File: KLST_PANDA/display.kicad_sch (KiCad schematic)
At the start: 10 parts, among them IC1 CAT4139TD-GT3, J6 FPC-40

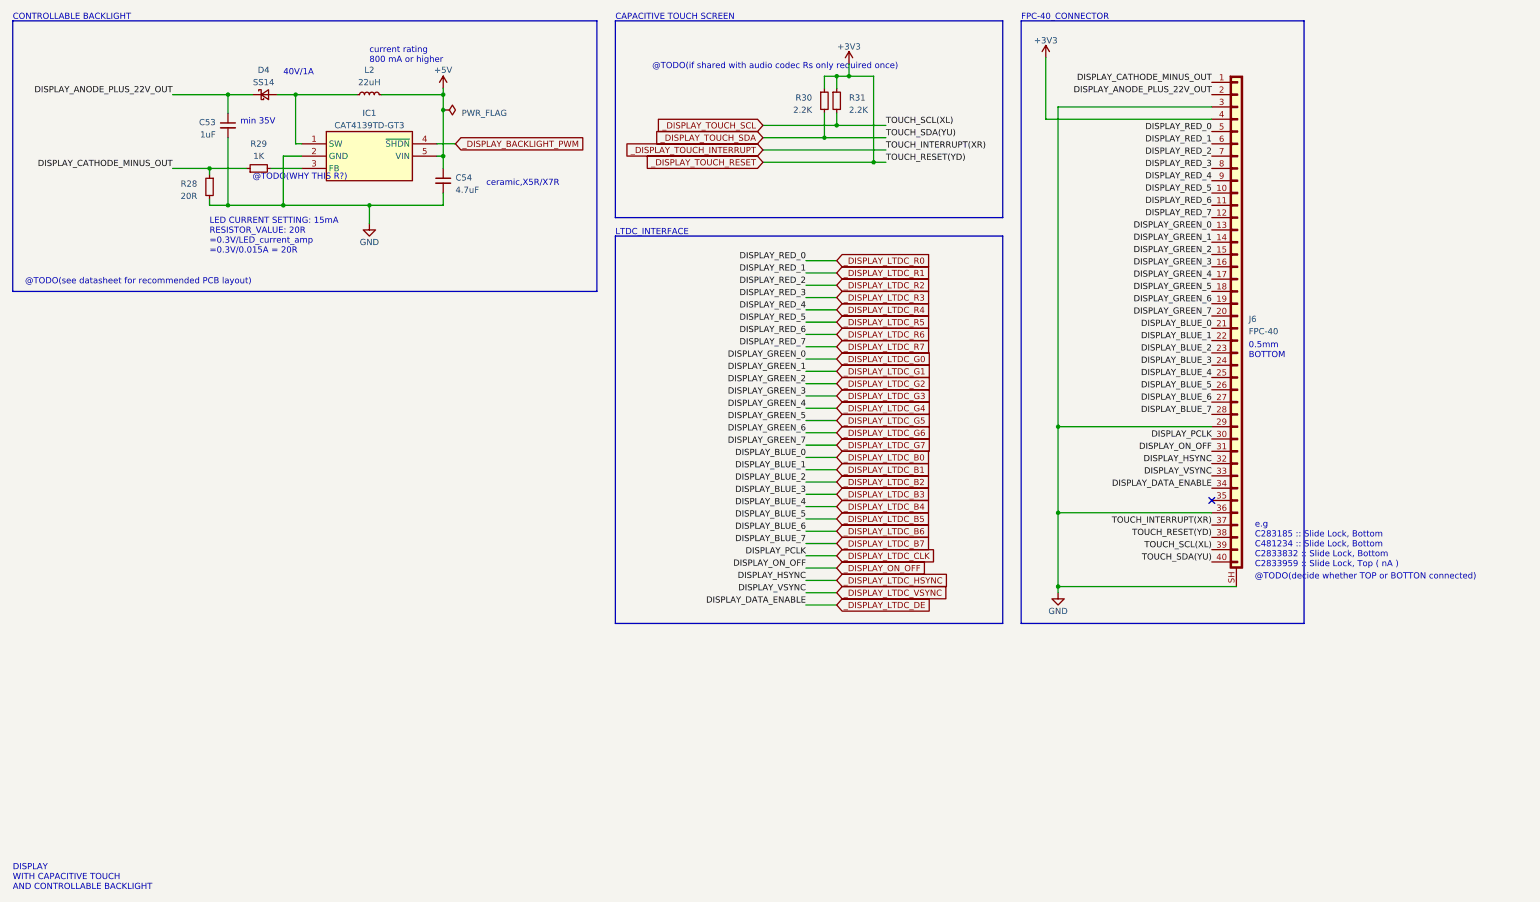
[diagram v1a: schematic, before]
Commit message: removed DRC warnings and error, added power page
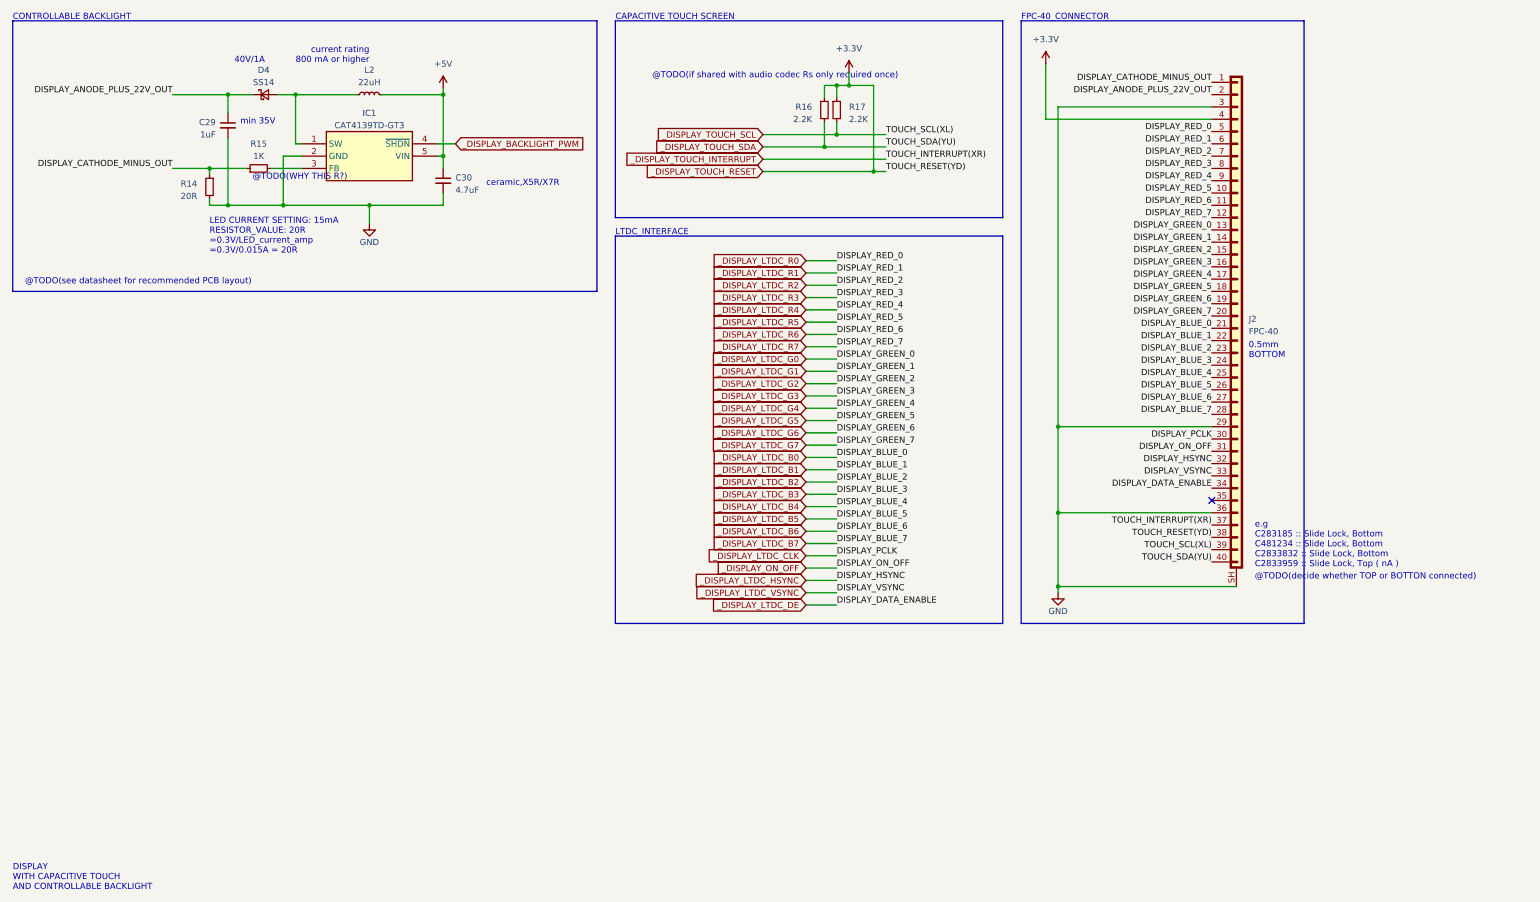
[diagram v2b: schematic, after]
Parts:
- renumbered C53 to C29, C54 to C30, J6 to J2, R28 to R14, R29 to R15, R30 to R16, R31 to R17
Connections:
- net +3V3 renamed +3.3V
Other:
- moved on the sheet: R16, R17

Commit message: changed I2C label, display can now be switched on and off
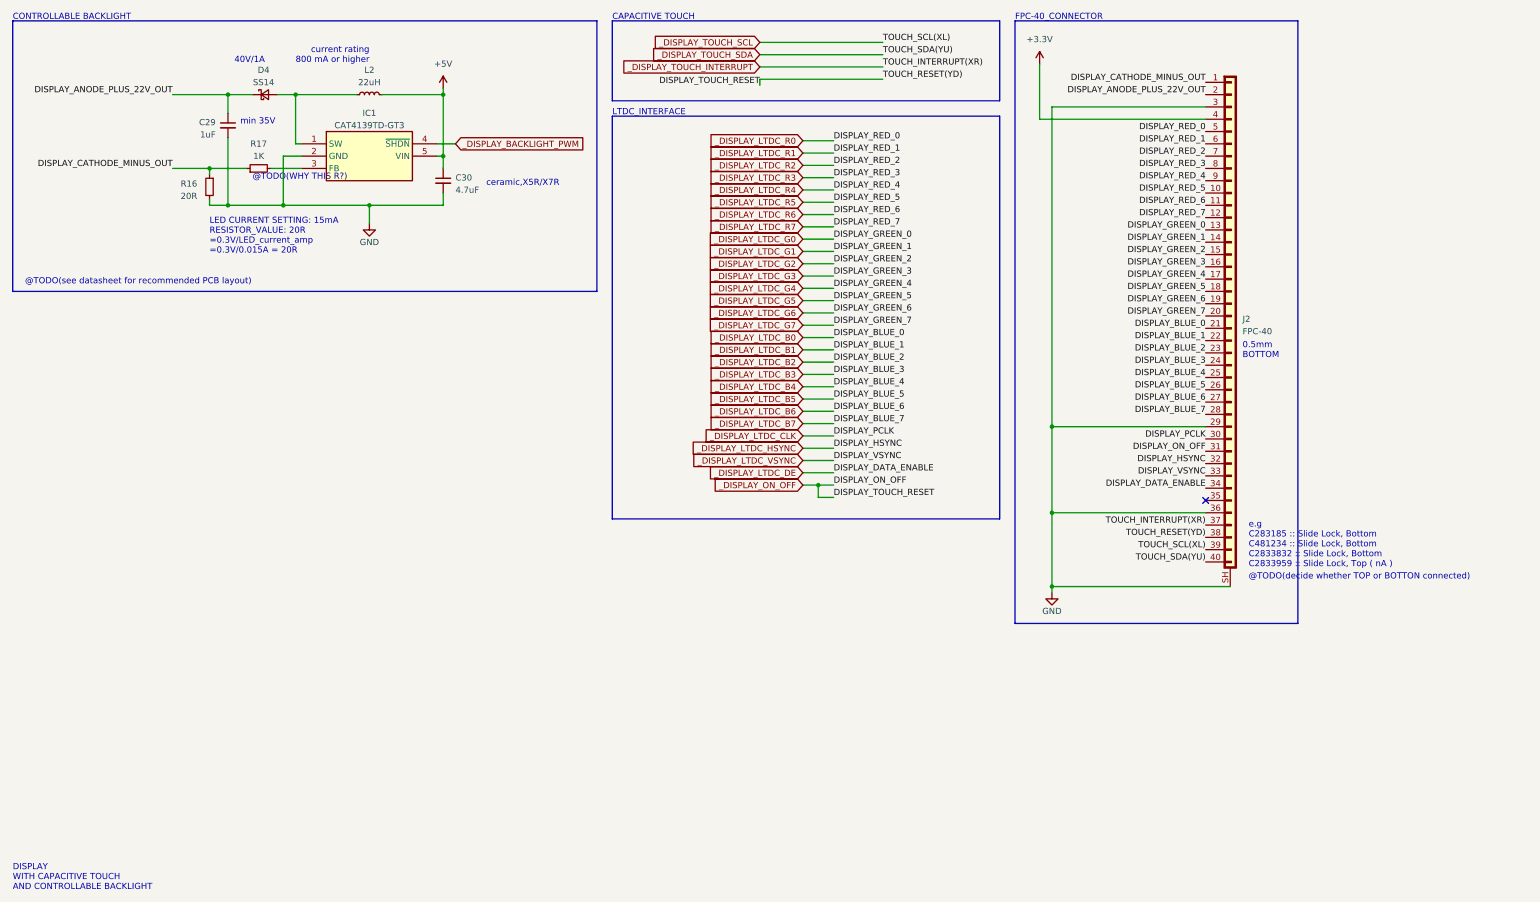
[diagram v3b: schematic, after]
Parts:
- removed R16, R17: 2.2K, symbol Device:R_Small
- renumbered R14 to R16, R15 to R17
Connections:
- net +3.3V: no longer J2.38 (Pin_38)
- net _DISPLAY_ON_OFF: now also J2.38 (Pin_38)
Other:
- note added: "CAPACITIVE TOUCH"
- note removed: "@TODO(if shared with audio codec Rs only required once)"
- note removed: "CAPACITIVE TOUCH SCREEN"
- moved on the sheet: J2

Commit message: cleaned up
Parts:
- renumbered R16 to R18, R17 to R19
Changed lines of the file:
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@@
   (symbol (lib_id "power:+5V") (at 104.14 29.21 0) (unit 1)
     (in_bom yes) (on_board yes) (dnp no) (fields_autoplaced)
-    (property "Reference" "#PWR043" (at 104.14 33.02 0)
+    (property "Reference" "#PWR044" (at 104.14 33.02 0)
       (effects (font (size 1.27 1.27)) hide)
     )
@@
       (project "KLST_PANDA"
         (path "/b4513875-4c57-4720-bcc5-43ead67fe18f/e5470bb0-cacd-4f1d-9ba6-63c7432dbe78"
-          (reference "#PWR043") (unit 1)
+          (reference "#PWR044") (unit 1)
         )
       )
@@
         )
         (path "/b4513875-4c57-4720-bcc5-43ead67fe18f/e5470bb0-cacd-4f1d-9ba6-63c7432dbe78"
-          (reference "#PWR045") (unit 1)
+          (reference "#PWR046") (unit 1)
         )
       )
@@
   (symbol (lib_id "Device:R_Small") (at 66.04 45.72 90) (unit 1)
     (in_bom yes) (on_board yes) (dnp no) (fields_autoplaced)
-    (property "Reference" "R17" (at 66.04 40.64 90)
+    (property "Reference" "R19" (at 66.04 40.64 90)
       (effects (font (size 1.27 1.27)))
     )
@@
       (project "KLST_PANDA"
         (path "/b4513875-4c57-4720-bcc5-43ead67fe18f/e5470bb0-cacd-4f1d-9ba6-63c7432dbe78"
-          (reference "R17") (unit 1)
+          (reference "R19") (unit 1)
         )
       )
@@
         )
         (path "/b4513875-4c57-4720-bcc5-43ead67fe18f/e5470bb0-cacd-4f1d-9ba6-63c7432dbe78"
-          (reference "#PWR044") (unit 1)
+          (reference "#PWR045") (unit 1)
         )
       )
@@
   (symbol (lib_id "Device:R_Small") (at 55.88 49.53 0) (mirror y) (unit 1)
     (in_bom yes) (on_board yes) (dnp no)
-    (property "Reference" "R16" (at 53.34 48.895 0)
+    (property "Reference" "R18" (at 53.34 48.895 0)
       (effects (font (size 1.27 1.27)) (justify left))
     )
@@
       (project "KLST_PANDA"
         (path "/b4513875-4c57-4720-bcc5-43ead67fe18f/e5470bb0-cacd-4f1d-9ba6-63c7432dbe78"
-          (reference "R16") (unit 1)
+          (reference "R18") (unit 1)
         )
       )
@@
         )
         (path "/b4513875-4c57-4720-bcc5-43ead67fe18f/e5470bb0-cacd-4f1d-9ba6-63c7432dbe78"
-          (reference "#PWR042") (unit 1)
-        )
-      )
+          (reference "#PWR043") (unit 1)
+        )
+      )

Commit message: unified internal I2C bus, cleaned up, added ESD protection to USB
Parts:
- renumbered C29 to C30, C30 to C31
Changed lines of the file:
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@@
   (symbol (lib_id "Device:C_Small") (at 104.14 48.26 0) (unit 1)
     (in_bom yes) (on_board yes) (dnp no) (fields_autoplaced)
-    (property "Reference" "C30" (at 106.68 47.6313 0)
+    (property "Reference" "C31" (at 106.68 47.6313 0)
       (effects (font (size 1.27 1.27)) (justify left))
     )
@@
       (project "KLST_PANDA"
         (path "/b4513875-4c57-4720-bcc5-43ead67fe18f/e5470bb0-cacd-4f1d-9ba6-63c7432dbe78"
+          (reference "C31") (unit 1)
+        )
+      )
+    )
+  )
+  (symbol (lib_id "Device:C_Small") (at 59.69 36.83 0) (mirror y) (unit 1)
+    (in_bom yes) (on_board yes) (dnp no)
+    (property "Reference" "C30" (at 57.15 36.2013 0)
+      (effects (font (size 1.27 1.27)) (justify left))
+    )
+    (property "Value" "1uF" (at 57.15 38.7413 0)
+      (effects (font (size 1.27 1.27)) (justify left))
+    )
+    (property "Footprint" "" (at 59.69 36.83 0)
+      (effects (font (size 1.27 1.27)) hide)
+    )
+    (property "Datasheet" "~" (at 59.69 36.83 0)
+      (effects (font (size 1.27 1.27)) hide)
+    )
+    (pin "1")
+    (pin "2")
+    (instances
+      (project "KLST_PANDA"
+        (path "/b4513875-4c57-4720-bcc5-43ead67fe18f/e5470bb0-cacd-4f1d-9ba6-63c7432dbe78"
           (reference "C30") (unit 1)
         )
@@
     )
   )
-  (symbol (lib_id "Device:C_Small") (at 59.69 36.83 0) (mirror y) (unit 1)
-    (in_bom yes) (on_board yes) (dnp no)
-    (property "Reference" "C29" (at 57.15 36.2013 0)
-      (effects (font (size 1.27 1.27)) (justify left))
-    )
-    (property "Value" "1uF" (at 57.15 38.7413 0)
-      (effects (font (size 1.27 1.27)) (justify left))
-    )
-    (property "Footprint" "" (at 59.69 36.83 0)
-      (effects (font (size 1.27 1.27)) hide)
-    )
-    (property "Datasheet" "~" (at 59.69 36.83 0)
-      (effects (font (size 1.27 1.27)) hide)
-    )
-    (pin "1")
-    (pin "2")
-    (instances
-      (project "KLST_PANDA"
-        (path "/b4513875-4c57-4720-bcc5-43ead67fe18f/e5470bb0-cacd-4f1d-9ba6-63c7432dbe78"
-          (reference "C29") (unit 1)
-        )
-      )
-    )
-  )
   (symbol (lib_id "power:+5V") (at 104.14 29.21 0) (unit 1)
     (in_bom yes) (on_board yes) (dnp no) (fields_autoplaced)
-    (property "Reference" "#PWR044" (at 104.14 33.02 0)
+    (property "Reference" "#PWR045" (at 104.14 33.02 0)
       (effects (font (size 1.27 1.27)) hide)
     )
@@
       (project "KLST_PANDA"
         (path "/b4513875-4c57-4720-bcc5-43ead67fe18f/e5470bb0-cacd-4f1d-9ba6-63c7432dbe78"
-          (reference "#PWR044") (unit 1)
+          (reference "#PWR045") (unit 1)
         )
       )
@@
         )
         (path "/b4513875-4c57-4720-bcc5-43ead67fe18f/e5470bb0-cacd-4f1d-9ba6-63c7432dbe78"
-          (reference "#PWR046") (unit 1)
+          (reference "#PWR047") (unit 1)
         )
       )
@@
         )
         (path "/b4513875-4c57-4720-bcc5-43ead67fe18f/e5470bb0-cacd-4f1d-9ba6-63c7432dbe78"
-          (reference "#PWR045") (unit 1)
+          (reference "#PWR046") (unit 1)
         )
       )
@@
         )
         (path "/b4513875-4c57-4720-bcc5-43ead67fe18f/e5470bb0-cacd-4f1d-9ba6-63c7432dbe78"
-          (reference "#PWR043") (unit 1)
-        )
-      )
+          (reference "#PWR044") (unit 1)
+        )
+      )

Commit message: resolved TODOs
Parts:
- renumbered IC1 to U3
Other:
- note added: "@NOTE(see datasheet p11 for recommended PCB layout)"
- note added: "ceramic, X5R/X7R close to VIN"
- note removed: "@TODO(WHY THIS R?)"
- note removed: "@TODO(decide whether TOP or BOTTON connected)"
- note removed: "@TODO(see datasheet for recommended PCB layout)"
- note removed: "LED CURRENT SETTING: 15mA RESISTOR_VALUE: 20R =0.3V/LED_current_amp =0.3V/0.015A = 20R"
- note removed: "ceramic,X5R/X7R"
- note removed: "e.g C283185 :: Slide Lock, Bottom C481234 :: Slide Lock, Bottom C2833832 :: Slide Lock, Bottom C2833959 :: Slide Lock, Top ( nA )"
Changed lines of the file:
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@@
     (fill (type none))
+  )
+  (text_box "using bottom-side connector THD0525-40CL-GF i.e if screen would be fitted on other side of the PCB a top-side connector would be required e.g JLCPCB(C2833959).\n( top side alternatives: C481234 + C2833832 )\n"
+    (at 222.25 139.7 0) (size 58.42 16.51)
+    (stroke (width 0) (type default))
+    (fill (type none))
+    (effects (font (size 1.27 1.27)) (justify left top))
+  )
+  (text_box "LED CURRENT SETTING: 15mA\nRESISTOR_VALUE: 20R\n=0.3V/LED_current_amp\n=0.3V/0.015A = 20R"
+    (at 55.88 55.245 0) (size 30.48 10.16)
+    (stroke (width 0) (type default))
+    (fill (type none))
+    (effects (font (size 1.27 1.27)) (justify left top))
   )
   (text "CONTROLLABLE BACKLIGHT" (at 15.24 15.24 0)
@@
     (effects (font (face "KiCad Font") (size 1.27 1.27)) (justify right bottom))
   )
-  (text "LED CURRENT SETTING: 15mA\nRESISTOR_VALUE: 20R\n=0.3V/LED_current_amp\n=0.3V/0.015A = 20R"
-    (at 55.88 63.5 0)
-    (effects (font (face "KiCad Font") (size 1.27 1.27)) (justify left bottom))
-  )
-  (text "e.g\nC283185 :: Slide Lock, Bottom\nC481234 :: Slide Lock, Bottom\nC2833832 :: Slide Lock, Bottom\nC2833959 :: Slide Lock, Top ( nA )"
-    (at 270.51 128.27 0)
-    (effects (font (face "KiCad Font") (size 1.27 1.27)) (justify left bottom))
-  )
-  (text "ceramic,X5R/X7R" (at 113.03 49.53 0)
-    (effects (font (face "KiCad Font") (size 1.27 1.27)) (justify left bottom))
-  )
-  (text "@TODO(decide whether TOP or BOTTON connected)" (at 270.51 130.81 0)
-    (effects (font (face "KiCad Font") (size 1.27 1.27)) (justify left bottom))
-  )
-  (text "@TODO(WHY THIS R?)" (at 64.77 48.26 0)
+  (text "ceramic, X5R/X7R\nclose to VIN" (at 113.03 50.165 0)
     (effects (font (face "KiCad Font") (size 1.27 1.27)) (justify left bottom))
   )
@@
     (effects (font (face "KiCad Font") (size 1.27 1.27)) (justify left bottom))
   )
-  (text "@TODO(see datasheet for recommended PCB layout)" (at 17.78 69.85 0)
+  (text "@NOTE(see datasheet p11 for recommended PCB layout)"
+    (at 18.415 67.945 0)
     (effects (font (face "KiCad Font") (size 1.27 1.27)) (justify left bottom))
   )
@@
   (symbol (lib_id "CAT4139TD-GT3:CAT4139TD-GT3") (at 74.93 40.64 0) (unit 1)
     (in_bom yes) (on_board yes) (dnp no)
-    (property "Reference" "IC1" (at 88.9 34.29 0)
+    (property "Reference" "U3" (at 88.9 34.29 0)
       (effects (font (size 1.27 1.27)))
     )
@@
       (project "KLST_PANDA"
         (path "/b4513875-4c57-4720-bcc5-43ead67fe18f/e5470bb0-cacd-4f1d-9ba6-63c7432dbe78"
-          (reference "IC1") (unit 1)
+          (reference "U3") (unit 1)
         )
       )
@@
   (symbol (lib_id "Device:R_Small") (at 55.88 49.53 0) (mirror y) (unit 1)
     (in_bom yes) (on_board yes) (dnp no)
-    (property "Reference" "R18" (at 53.34 48.895 0)
+    (property "Reference" "R18" (at 54.61 48.895 0)
       (effects (font (size 1.27 1.27)) (justify left))
     )
-    (property "Value" "20R" (at 53.34 51.435 0)
+    (property "Value" "20R" (at 54.61 50.8 0)
       (effects (font (size 1.27 1.27)) (justify left))
     )

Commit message: started spec'ing components
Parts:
- C30: footprint (none) -> Capacitor_SMD:C_0402_1005Metric; JLCPCB (none) -> C52923
- C31: footprint (none) -> Capacitor_SMD:C_0402_1005Metric; JLCPCB (none) -> C23733
- D4: footprint (none) -> Diode_SMD:D_SMA; JLCPCB (none) -> C2480; JLCPCB Part # C2480 -> (none)
- J2: JLCPCB (none) -> C283185; JLCPCB Part # C283185 -> (none)
- L2: footprint (none) -> Inductor_SMD:L_Changjiang_FNR4030S; JLCPCB (none) -> C167883; JLCPCB Part # C112330 -> (none)
- R18: JLCPCB (none) -> TODO
- R19: footprint (none) -> Resistor_SMD:R_0805_2012Metric_Pad1.20x1.40mm_HandSolder; JLCPCB (none) -> C17513
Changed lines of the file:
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@@
       (effects (font (size 1.27 1.27)) (justify left))
     )
-    (property "Footprint" "" (at 104.14 48.26 0)
+    (property "Footprint" "Capacitor_SMD:C_0402_1005Metric" (at 104.14 48.26 0)
       (effects (font (size 1.27 1.27)) hide)
     )
@@
       (effects (font (size 1.27 1.27)) hide)
     )
+    (property "Description" "10V" (at 104.14 48.26 0)
+      (effects (font (size 1.27 1.27)) hide)
+    )
+    (property "JLCPCB" "C23733" (at 104.14 48.26 0)
+      (effects (font (size 1.27 1.27)) hide)
+    )
     (pin "1")
     (pin "2")
@@
       (effects (font (size 1.27 1.27)) (justify left))
     )
-    (property "Footprint" "" (at 59.69 36.83 0)
+    (property "Footprint" "Capacitor_SMD:C_0402_1005Metric" (at 59.69 36.83 0)
       (effects (font (size 1.27 1.27)) hide)
     )
     (property "Datasheet" "~" (at 59.69 36.83 0)
+      (effects (font (size 1.27 1.27)) hide)
+    )
+    (property "JLCPCB Part #" "" (at 59.69 36.83 0)
+      (effects (font (size 1.27 1.27)) hide)
+    )
+    (property "JLCPCB" "C52923" (at 59.69 36.83 0)
+      (effects (font (size 1.27 1.27)) hide)
+    )
+    (property "Description" "25V" (at 59.69 36.83 0)
       (effects (font (size 1.27 1.27)) hide)
     )
@@
       (effects (font (size 1.27 1.27)))
     )
-    (property "Footprint" "" (at 67.31 30.48 90)
+    (property "Footprint" "Diode_SMD:D_SMA" (at 67.31 30.48 90)
       (effects (font (size 1.27 1.27)) hide)
     )
@@
       (effects (font (size 1.27 1.27)) hide)
     )
-    (property "JLCPCB Part #" "C2480" (at 67.31 30.48 0)
+    (property "JLCPCB Part #" "" (at 67.31 30.48 0)
+      (effects (font (size 1.27 1.27)) hide)
+    )
+    (property "JLCPCB" "C2480" (at 67.31 30.48 0)
       (effects (font (size 1.27 1.27)) hide)
     )
@@
       (effects (font (size 1.27 1.27)))
     )
-    (property "Footprint" "" (at 66.04 45.72 0)
+    (property "Footprint" "Resistor_SMD:R_0805_2012Metric_Pad1.20x1.40mm_HandSolder" (at 66.04 45.72 0)
       (effects (font (size 1.27 1.27)) hide)
     )
@@
       (effects (font (size 1.27 1.27)) hide)
     )
+    (property "JLCPCB" "C17513" (at 66.04 45.72 0)
+      (effects (font (size 1.27 1.27)) hide)
+    )
     (pin "1")
     (pin "2")
@@
       (effects (font (size 1.27 1.27)) hide)
     )
-    (property "JLCPCB Part #" "C283185" (at 266.7 76.2 0)
+    (property "JLCPCB Part #" "" (at 266.7 76.2 0)
+      (effects (font (size 1.27 1.27)) hide)
+    )
+    (property "JLCPCB" "C283185" (at 266.7 76.2 0)
       (effects (font (size 1.27 1.27)) hide)
     )
@@
       (effects (font (size 1.27 1.27)) hide)
     )
+    (property "JLCPCB" "TODO" (at 55.88 49.53 0)
+      (effects (font (size 1.27 1.27)) hide)
+    )
     (pin "1")
     (pin "2")
@@
       (effects (font (size 1.27 1.27)))
     )
-    (property "Footprint" "" (at 88.9 30.48 0)
+    (property "Footprint" "Inductor_SMD:L_Changjiang_FNR4030S" (at 88.9 30.48 0)
       (effects (font (size 1.27 1.27)) hide)
     )
@@
       (effects (font (size 1.27 1.27)) hide)
     )
-    (property "JLCPCB Part #" "C112330" (at 88.9 30.48 90)
-      (effects (font (size 1.27 1.27)) hide)
-    )
+    (property "JLCPCB Part #" "" (at 88.9 30.48 90)
+      (effects (font (size 1.27 1.27)) hide)
+    )
+    (property "JLCPCB" "C167883" (at 88.9 30.48 0)
+      (effects (font (size 1.27 1.27)) hide)
+    )
+    (property "Description" "1A" (at 88.9 30.48 0)
+      (effects (font (size 1.27 1.27)) hide)
+    )
